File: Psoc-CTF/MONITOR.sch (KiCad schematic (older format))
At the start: 16 parts

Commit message: Generación de lista de materiales
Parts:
- gave numbers to parts that had none: 16
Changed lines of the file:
@@
 $EndDescr
 $Comp
-L RF_Module:ESP32-WROOM-32D U?
+L RF_Module:ESP32-WROOM-32D U3
 U 1 1 621CC162
 P 1800 2350
-F 0 "U?" H 2300 900 50  0000 C CNN
+F 0 "U3" H 2300 900 50  0000 C CNN
 F 1 "ESP32-WROOM-32D" H 2300 1000 50  0000 C CNN
 F 2 "RF_Module:ESP32-WROOM-32" H 1800 850 50  0001 C CNN
@@
 $EndComp
 $Comp
-L Device:C C?
+L Device:C C7
 U 1 1 621D2118
 P 3400 950
-F 0 "C?" H 3515 996 50  0000 L CNN
+F 0 "C7" H 3515 996 50  0000 L CNN
 F 1 "10uF" H 3515 905 50  0000 L CNN
 F 2 "Capacitor_SMD:C_0805_2012Metric_Pad1.18x1.45mm_HandSolder" H 3438 800 50  0001 C CNN
@@
 $EndComp
 $Comp
-L Device:C C?
+L Device:C C8
 U 1 1 621D24F4
 P 3800 950
-F 0 "C?" H 3915 996 50  0000 L CNN
+F 0 "C8" H 3915 996 50  0000 L CNN
 F 1 "1uF" H 3915 905 50  0000 L CNN
 F 2 "Capacitor_SMD:C_0603_1608Metric_Pad1.08x0.95mm_HandSolder" H 3838 800 50  0001 C CNN
@@
 $EndComp
 $Comp
-L Device:C C?
+L Device:C C9
 U 1 1 621D2B1C
 P 4200 950
-F 0 "C?" H 4315 996 50  0000 L CNN
+F 0 "C9" H 4315 996 50  0000 L CNN
 F 1 "0.1uF" H 4315 905 50  0000 L CNN
 F 2 "Capacitor_SMD:C_0603_1608Metric_Pad1.08x0.95mm_HandSolder" H 4238 800 50  0001 C CNN
@@
 Connection ~ 3800 1100
 $Comp
-L power:VDD #PWR?
+L power:VDD #PWR016
 U 1 1 621E240B
 P 3800 800
-F 0 "#PWR?" H 3800 650 50  0001 C CNN
+F 0 "#PWR016" H 3800 650 50  0001 C CNN
 F 1 "VDD" H 3815 973 50  0000 C CNN
 F 2 "" H 3800 800 50  0001 C CNN
@@
 $EndComp
 $Comp
-L power:VDD #PWR?
+L power:VDD #PWR013
 U 1 1 621E27EB
 P 1800 900
-F 0 "#PWR?" H 1800 750 50  0001 C CNN
+F 0 "#PWR013" H 1800 750 50  0001 C CNN
 F 1 "VDD" H 1815 1073 50  0000 C CNN
 F 2 "" H 1800 900 50  0001 C CNN
@@
 	1800 900  1800 950
 $Comp
-L power:GND #PWR?
+L power:GND #PWR017
 U 1 1 621E322C
 P 3800 1200
-F 0 "#PWR?" H 3800 950 50  0001 C CNN
+F 0 "#PWR017" H 3800 950 50  0001 C CNN
 F 1 "GND" H 3805 1027 50  0000 C CNN
 F 2 "" H 3800 1200 50  0001 C CNN
@@
 	3800 1100 3800 1200
 $Comp
-L power:GND #PWR?
+L power:GND #PWR014
 U 1 1 621E3647
 P 1800 3750
-F 0 "#PWR?" H 1800 3500 50  0001 C CNN
+F 0 "#PWR014" H 1800 3500 50  0001 C CNN
 F 1 "GND" H 1805 3577 50  0000 C CNN
 F 2 "" H 1800 3750 50  0001 C CNN
@@
 $EndComp
 $Comp
-L Device:R R?
+L Device:R R2
 U 1 1 621E4581
 P 800 1000
-F 0 "R?" H 870 1046 50  0000 L CNN
+F 0 "R2" H 870 1046 50  0000 L CNN
 F 1 "10K" H 870 955 50  0000 L CNN
 F 2 "Resistor_SMD:R_0603_1608Metric_Pad0.98x0.95mm_HandSolder" V 730 1000 50  0001 C CNN
@@
 $EndComp
 $Comp
-L Device:C C?
+L Device:C C6
 U 1 1 621E49B9
 P 800 1300
-F 0 "C?" H 915 1346 50  0000 L CNN
+F 0 "C6" H 915 1346 50  0000 L CNN
 F 1 "0.1uF" H 915 1255 50  0000 L CNN
 F 2 "Capacitor_SMD:C_0603_1608Metric_Pad1.08x0.95mm_HandSolder" H 838 1150 50  0001 C CNN
@@
 Connection ~ 800  1150
 $Comp
-L power:GND #PWR?
+L power:GND #PWR012
 U 1 1 621E4F01
 P 800 1450
-F 0 "#PWR?" H 800 1200 50  0001 C CNN
+F 0 "#PWR012" H 800 1200 50  0001 C CNN
 F 1 "GND" H 805 1277 50  0000 C CNN
 F 2 "" H 800 1450 50  0001 C CNN
@@
 $EndComp
 $Comp
-L power:VDD #PWR?
+L power:VDD #PWR011
 U 1 1 621E53C7
 P 800 850
-F 0 "#PWR?" H 800 700 50  0001 C CNN
+F 0 "#PWR011" H 800 700 50  0001 C CNN
 F 1 "VDD" H 815 1023 50  0000 C CNN
 F 2 "" H 800 850 50  0001 C CNN
@@
 $EndComp
 $Comp
-L Connector_Generic:Conn_02x03_Odd_Even J?
+L Connector_Generic:Conn_02x03_Odd_Even J3
 U 1 1 621E61BE
 P 1750 4550
-F 0 "J?" H 1800 4850 50  0000 C CNN
+F 0 "J3" H 1800 4850 50  0000 C CNN
 F 1 "PROG" H 1800 4776 50  0000 C CNN
 F 2 "Connector_PinHeader_2.54mm:PinHeader_2x03_P2.54mm_Vertical" H 1750 4550 50  0001 C CNN
@@
 	2150 4550 2150 4650
 $Comp
-L power:GND #PWR?
+L power:GND #PWR015
 U 1 1 621E7CEF
 P 2150 4650
-F 0 "#PWR?" H 2150 4400 50  0001 C CNN
+F 0 "#PWR015" H 2150 4400 50  0001 C CNN
 F 1 "GND" H 2155 4477 50  0000 C CNN
 F 2 "" H 2150 4650 50  0001 C CNN
@@
 U2_TX
 $Comp
-L SST25VF512:SST25VF512-20-4C-SAE U?
+L SST25VF512:SST25VF512-20-4C-SAE U5
 U 1 1 621FA958
 P 7050 1950
-F 0 "U?" H 8250 2337 60  0000 C CNN
+F 0 "U5" H 8250 2337 60  0000 C CNN
 F 1 "SST25VF512-20-4C-SAE" H 8250 2231 60  0000 C CNN
 F 2 "Psoc-CTF:SST25VF512-20-4C-SAE" H 8250 2190 60  0001 C CNN
@@
 $EndComp
 $Comp
-L 23LC1024:23LC1024-E_SN U?
+L 23LC1024:23LC1024-E_SN U4
 U 1 1 621FC9CB
 P 6400 3650
-F 0 "U?" H 8000 4037 60  0000 C CNN
+F 0 "U4" H 8000 4037 60  0000 C CNN
 F 1 "23LC1024-E_SN" H 8000 3931 60  0000 C CNN
 F 2 "Psoc-CTF:23LC1024-E&slash_SN" H 8000 3890 60  0001 C CNN
@@
 $EndComp
 $Comp
-L power:VDD #PWR?
+L power:VDD #PWR025
 U 1 1 621FD5AD
 P 9500 1900
-F 0 "#PWR?" H 9500 1750 50  0001 C CNN
+F 0 "#PWR025" H 9500 1750 50  0001 C CNN
 F 1 "VDD" H 9515 2073 50  0000 C CNN
 F 2 "" H 9500 1900 50  0001 C CNN
@@
 	9500 1950 9450 1950
 $Comp
-L power:VDD #PWR?
+L power:VDD #PWR026
 U 1 1 621FE9ED
 P 9700 3600
-F 0 "#PWR?" H 9700 3450 50  0001 C CNN
+F 0 "#PWR026" H 9700 3450 50  0001 C CNN
 F 1 "VDD" H 9715 3773 50  0000 C CNN
 F 2 "" H 9700 3600 50  0001 C CNN
@@
 	9700 3650 9600 3650
 $Comp
-L power:GND #PWR?
+L power:GND #PWR018
 U 1 1 621FFBEC
 P 6300 4000
-F 0 "#PWR?" H 6300 3750 50  0001 C CNN
+F 0 "#PWR018" H 6300 3750 50  0001 C CNN
 F 1 "GND" H 6305 3827 50  0000 C CNN
 F 2 "" H 6300 4000 50  0001 C CNN
@@
 	6300 3950 6300 4000
 $Comp
-L power:GND #PWR?
+L power:GND #PWR020
 U 1 1 6220272F
 P 7000 2300
-F 0 "#PWR?" H 7000 2050 50  0001 C CNN
+F 0 "#PWR020" H 7000 2050 50  0001 C CNN
 F 1 "GND" H 7005 2127 50  0000 C CNN
 F 2 "" H 7000 2300 50  0001 C CNN
@@
 	7000 2250 7050 2250
 $Comp
-L Device:C C?
+L Device:C C10
 U 1 1 622042DD
 P 7700 1050
-F 0 "C?" H 7815 1096 50  0000 L CNN
+F 0 "C10" H 7815 1096 50  0000 L CNN
 F 1 "1uF" H 7815 1005 50  0000 L CNN
 F 2 "Capacitor_SMD:C_0603_1608Metric_Pad1.08x0.95mm_HandSolder" H 7738 900 50  0001 C CNN
@@
 $EndComp
 $Comp
-L Device:C C?
+L Device:C C12
 U 1 1 622042E3
 P 8100 1050
-F 0 "C?" H 8215 1096 50  0000 L CNN
+F 0 "C12" H 8215 1096 50  0000 L CNN
 F 1 "0.1uF" H 8215 1005 50  0000 L CNN
 F 2 "Capacitor_SMD:C_0603_1608Metric_Pad1.08x0.95mm_HandSolder" H 8138 900 50  0001 C CNN
@@
 Connection ~ 7700 1200
 $Comp
-L power:VDD #PWR?
+L power:VDD #PWR021
 U 1 1 622042EF
 P 7700 900
-F 0 "#PWR?" H 7700 750 50  0001 C CNN
+F 0 "#PWR021" H 7700 750 50  0001 C CNN
 F 1 "VDD" H 7715 1073 50  0000 C CNN
 F 2 "" H 7700 900 50  0001 C CNN
@@
 $EndComp
 $Comp
-L power:GND #PWR?
+L power:GND #PWR022
 U 1 1 622042F5
 P 7700 1300
-F 0 "#PWR?" H 7700 1050 50  0001 C CNN
+F 0 "#PWR022" H 7700 1050 50  0001 C CNN
 F 1 "GND" H 7705 1127 50  0000 C CNN
 F 2 "" H 7700 1300 50  0001 C CNN
@@
 	7700 1200 7700 1300
 $Comp
-L Device:C C?
+L Device:C C11
 U 1 1 62206F44
 P 8000 4600
-F 0 "C?" H 8115 4646 50  0000 L CNN
+F 0 "C11" H 8115 4646 50  0000 L CNN
 F 1 "1uF" H 8115 4555 50  0000 L CNN
 F 2 "Capacitor_SMD:C_0603_1608Metric_Pad1.08x0.95mm_HandSolder" H 8038 4450 50  0001 C CNN
@@
 $EndComp
 $Comp
-L Device:C C?
+L Device:C C13
 U 1 1 62206F4A
 P 8400 4600
-F 0 "C?" H 8515 4646 50  0000 L CNN
+F 0 "C13" H 8515 4646 50  0000 L CNN
 F 1 "0.1uF" H 8515 4555 50  0000 L CNN
 F 2 "Capacitor_SMD:C_0603_1608Metric_Pad1.08x0.95mm_HandSolder" H 8438 4450 50  0001 C CNN
@@
 Connection ~ 8000 4750
 $Comp
-L power:VDD #PWR?
+L power:VDD #PWR023
 U 1 1 62206F54
 P 8000 4450
-F 0 "#PWR?" H 8000 4300 50  0001 C CNN
+F 0 "#PWR023" H 8000 4300 50  0001 C CNN
 F 1 "VDD" H 8015 4623 50  0000 C CNN
 F 2 "" H 8000 4450 50  0001 C CNN
@@
 $EndComp
 $Comp
-L power:GND #PWR?
+L power:GND #PWR024
 U 1 1 62206F5A
 P 8000 4850
-F 0 "#PWR?" H 8000 4600 50  0001 C CNN
+F 0 "#PWR024" H 8000 4600 50  0001 C CNN
 F 1 "GND" H 8005 4677 50  0000 C CNN
 F 2 "" H 8000 4850 50  0001 C CNN
@@
 SPI_MISO
 $Comp
-L Device:R R?
+L Device:R R3
 U 1 1 622253DD
 P 6700 2300
-F 0 "R?" H 6770 2346 50  0000 L CNN
+F 0 "R3" H 6770 2346 50  0000 L CNN
 F 1 "0" H 6770 2255 50  0000 L CNN
 F 2 "Resistor_SMD:R_0603_1608Metric_Pad0.98x0.95mm_HandSolder" V 6630 2300 50  0001 C CNN
@@
 $EndComp
 $Comp
-L power:GND #PWR?
+L power:GND #PWR019
 U 1 1 62225D99
 P 6700 2450
-F 0 "#PWR?" H 6700 2200 50  0001 C CNN
+F 0 "#PWR019" H 6700 2200 50  0001 C CNN
 F 1 "GND" H 6705 2277 50  0000 C CNN
 F 2 "" H 6700 2450 50  0001 C CNN
@@
 $EndComp
 $Comp
-L Device:R R?
+L Device:R R4
 U 1 1 622266CA
 P 9800 1900
-F 0 "R?" H 9650 1950 50  0000 L CNN
+F 0 "R4" H 9650 1950 50  0000 L CNN
 F 1 "10K" H 9600 1850 50  0000 L CNN
 F 2 "Resistor_SMD:R_0603_1608Metric_Pad0.98x0.95mm_HandSolder" V 9730 1900 50  0001 C CNN
@@
 $EndComp
 $Comp
-L power:VDD #PWR?
+L power:VDD #PWR027
 U 1 1 62226EED
 P 9800 1750
-F 0 "#PWR?" H 9800 1600 50  0001 C CNN
+F 0 "#PWR027" H 9800 1600 50  0001 C CNN
 F 1 "VDD" H 9815 1923 50  0000 C CNN
 F 2 "" H 9800 1750 50  0001 C CNN
@@
 $EndComp
 $Comp
-L Device:R R?
+L Device:R R5
 U 1 1 622274B9
 P 9950 3600
-F 0 "R?" H 9800 3650 50  0000 L CNN
+F 0 "R5" H 9800 3650 50  0000 L CNN
 F 1 "10K" H 9750 3550 50  0000 L CNN
 F 2 "Resistor_SMD:R_0603_1608Metric_Pad0.98x0.95mm_HandSolder" V 9880 3600 50  0001 C CNN
@@
 	9600 3750 9950 3750
 $Comp
-L power:VDD #PWR?
+L power:VDD #PWR028
 U 1 1 622296DD
 P 9950 3450
-F 0 "#PWR?" H 9950 3300 50  0001 C CNN
+F 0 "#PWR028" H 9950 3300 50  0001 C CNN
 F 1 "VDD" H 9965 3623 50  0000 C CNN
 F 2 "" H 9950 3450 50  0001 C CNN

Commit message: Se retira las memorias flash y Ram por spi y se coloca una F-RAM por i2c
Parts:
- removed C10, C11: 1uF, Capacitor_SMD:C_0603_1608Metric_Pad1.08x0.95mm_HandSolder, symbol Device:C
- removed C12, C13: 0.1uF, Capacitor_SMD:C_0603_1608Metric_Pad1.08x0.95mm_HandSolder, symbol Device:C
- removed R3: 0, Resistor_SMD:R_0603_1608Metric_Pad0.98x0.95mm_HandSolder, symbol Device:R
- removed U4: 23LC1024-E_SN, Psoc-CTF:23LC1024-E&slash_SN, symbol 23LC1024:23LC1024-E_SN
- removed U5: SST25VF512-20-4C-SAE, Psoc-CTF:SST25VF512-20-4C-SAE, symbol SST25VF512:SST25VF512-20-4C-SAE
- renumbered R2 to R3
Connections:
- net labels added: SCL, SDA, T_MCU_SCL, T_MCU_SDA
- net labels removed: CE_FLASH, CE_RAM, SPI_CLK, SPI_MISO, SPI_MOSI
- wire segments 49 -> 25
- no-connect marks 23 -> 25
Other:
- note added: "I2C MONITOR"
- note added: "MONITOR MCU"
- note added: "PROGRAMMING"
- note removed: "MEMORY FLASH"
- note removed: "MEMORY RAM\n"

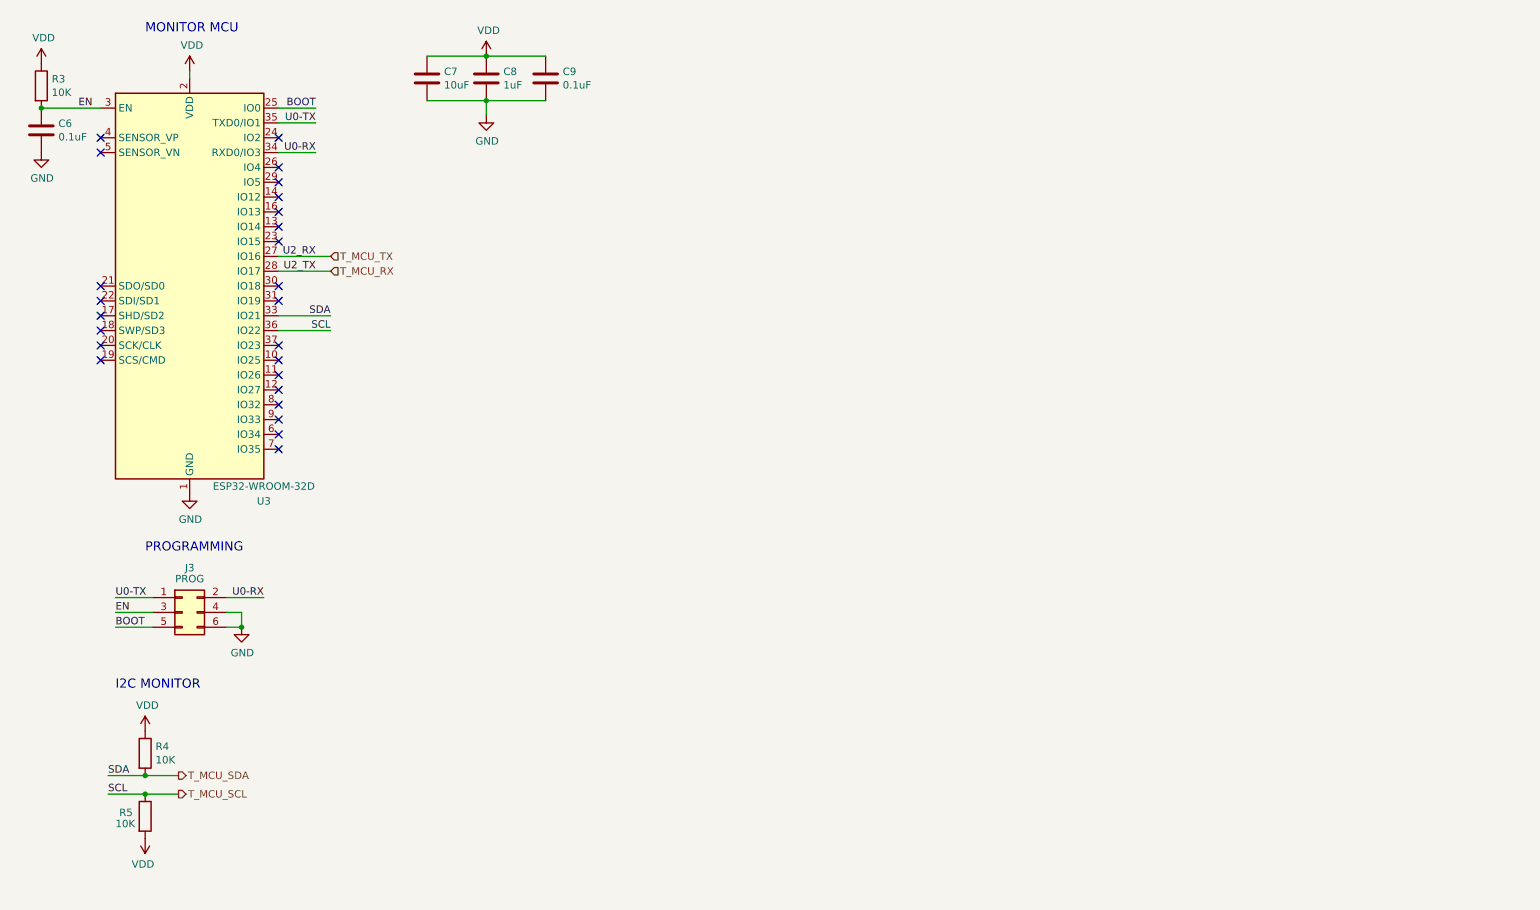
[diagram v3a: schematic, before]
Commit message: Antena agregada, pines de programación SWD
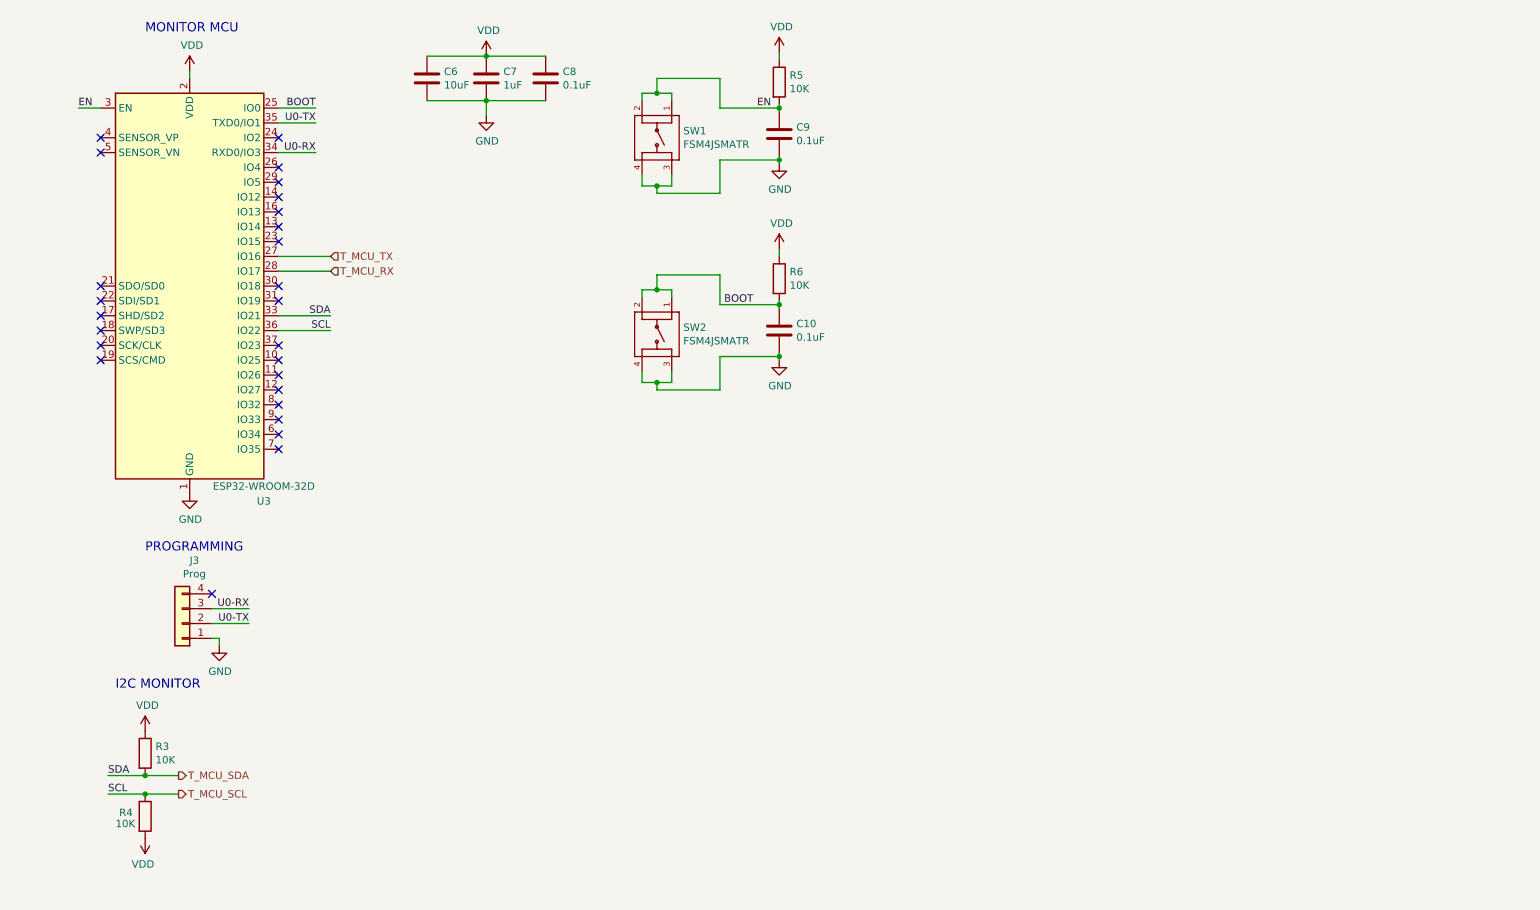
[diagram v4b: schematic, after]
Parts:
- removed J3: PROG, Connector_PinHeader_2.54mm:PinHeader_2x03_P2.54mm_Vertical, symbol Connector_Generic:Conn_02x03_Odd_Even
- added C10: 0.1uF, Capacitor_SMD:C_0603_1608Metric_Pad1.08x0.95mm_HandSolder, symbol Device:C
- added J3: Prog, Connector_PinHeader_2.54mm:PinHeader_1x04_P2.54mm_Vertical, symbol Connector_Generic:Conn_01x04
- added R6: 10K, Resistor_SMD:R_0603_1608Metric_Pad0.98x0.95mm_HandSolder, symbol Device:R
- added SW1, SW2: FSM4JSMATR, Psoc-CTF:Push_button_FSM4JSMATR, symbol Push_button_FSM4JSMATR:4-1437565-2
- renumbered C7 to C6, C8 to C7, C9 to C8, C6 to C9, R4 to R3, R5 to R4, R3 to R5
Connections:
- net BOOT: now also C10.1, R6.2, SW2.1, SW2.2
- net EN: now also SW1.1, SW1.2
- net GND: now also C10.2, J3.1 (Pin_1), SW1.3, SW1.4, SW2.3, SW2.4
- net U0-RX: now also J3.3 (Pin_3)
- net U0-TX: now also J3.2 (Pin_2)
- net VDD: now also R6.1
- no-connect marks 25 -> 26
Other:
- moved on the sheet: C9, R5

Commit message: Ruteo Psoc-CTF
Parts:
- added C42, C44: 1uF, Capacitor_SMD:C_0603_1608Metric_Pad1.08x0.95mm_HandSolder, symbol Device:C
- added C43, C45: 0.1uF, Capacitor_SMD:C_0603_1608Metric_Pad1.08x0.95mm_HandSolder, symbol Device:C
- added D10, D9: LED, LED_SMD:LED_0603_1608Metric_Pad1.05x0.95mm_HandSolder, symbol Device:LED
- added D11: SSA14, Diode_SMD:D_SMA_Handsoldering, symbol Device:D_Schottky
- added J12: USB3076-XX-X_REVC, Psoc-CTF:microUSB, symbol microUSB:USB3076-XX-X_REVC
- added R43: 10k, Resistor_SMD:R_0603_1608Metric_Pad0.98x0.95mm_HandSolder, symbol Device:R
- added R44, R45: 1K, Resistor_SMD:R_0603_1608Metric_Pad0.98x0.95mm_HandSolder, symbol Device:R
- added U7: CY7C65211-24LTXI, Package_DFN_QFN:QFN-24-1EP_4x4mm_P0.5mm_EP2.6x2.6mm, symbol Interface_USB:CY7C65211-24LTXI
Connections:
- net GND: now also C42.2, C43.2, C44.2, C45.2, J12.5 (GND), U7.13 (VSSD), U7.16 (VSSD), U7.17 (VSSA), U7.3 (VSSD)
- net VDD: now also R44.1, R45.1; no longer C6.1, C7.1, C8.1, R3.1, R4.2, R5.1, R6.1, U3.2 (VDD)
- net U0-RX renamed RXD
- net RXD: now also U3.35 (TXD0/IO1), U7.1 (SCB_0/GPIO_6); no longer U3.34 (RXD0/IO3)
- net U0-TX renamed TXD
- net TXD: now also U3.34 (RXD0/IO3), U7.23 (SCB_4/GPIO_5); no longer U3.35 (TXD0/IO1)
- new net: C42.1, U7.12 (VCCD)
- new net: R43.2, U7.14 (~XRES)
- new net: D10.1 (K), U7.4 (GPIO_8)
- new net: D9.1 (K), U7.5 (GPIO_9)
- new net: D9.2 (A), R44.2
- new net: D10.2 (A), R45.2
- new net: D11.2 (A), J12.1 (VBUS)
- new net +3V3: C44.1, C45.1, C6.1, C7.1, C8.1, R3.1, R4.2, R43.1, R5.1, R6.1, U3.2 (VDD), U7.24 (VDDD)
- new net D+: J12.3 (D+), U7.10 (USBDP)
- new net D-: J12.2 (D-), U7.11 (USBDM)
- new net Earth: C43.1, J12.10 (SHIELD), J12.11 (SHIELD), J12.6 (SHIELD), J12.7 (SHIELD), J12.8 (SHIELD), J12.9 (SHIELD)
- new net VBUS: D11.1 (K), U7.15 (VBUS)
- no-connect marks 26 -> 37
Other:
- note added: "FTDI TO MCU\n"
- note added: "USB TO TTL"

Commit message: Corrrecciones y anexo de logo
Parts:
- removed C10: 0.1uF, Capacitor_SMD:C_0603_1608Metric_Pad1.08x0.95mm_HandSolder, symbol Device:C
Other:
- moved on the sheet: C42, C43, C44, C45, D10, D11, D9, J12, R3, R4, R43, R44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

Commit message: Correcciones del retorno de tiera y medicion de corriente
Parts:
- J3: footprint Connector_PinHeader_2.54mm:PinHeader_1x04_P2.54mm_Vertical -> Connector_PinHeader_2.54mm:PinHeader_2x02_P2.54mm_Vertical
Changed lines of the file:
@@
 F 0 "J3" H 1668 4200 50  0000 C CNN
 F 1 "Prog" H 1668 4291 50  0000 C CNN
-F 2 "Connector_PinHeader_2.54mm:PinHeader_1x04_P2.54mm_Vertical" H 1750 4625 50  0001 C CNN
+F 2 "Connector_PinHeader_2.54mm:PinHeader_2x02_P2.54mm_Vertical" H 1750 4625 50  0001 C CNN
 F 3 "~" H 1750 4625 50  0001 C CNN
 	1    1750 4625
